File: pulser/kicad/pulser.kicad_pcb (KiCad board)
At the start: 2 copper layers, 90 x 70 mm, 46 parts, among them J1 Screw_Terminal_01x02, J2 Screw_Terminal_01x02, J3 Conn_01x06_Male, J4 Screw_Terminal_01x02, J5 Conn_01x07_Male, Q1 RQ6E080AJTCR, Q2 RQ6E080AJTCR, SW1 SW_Push, SW2 SW_Push, SW3 SW_Push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

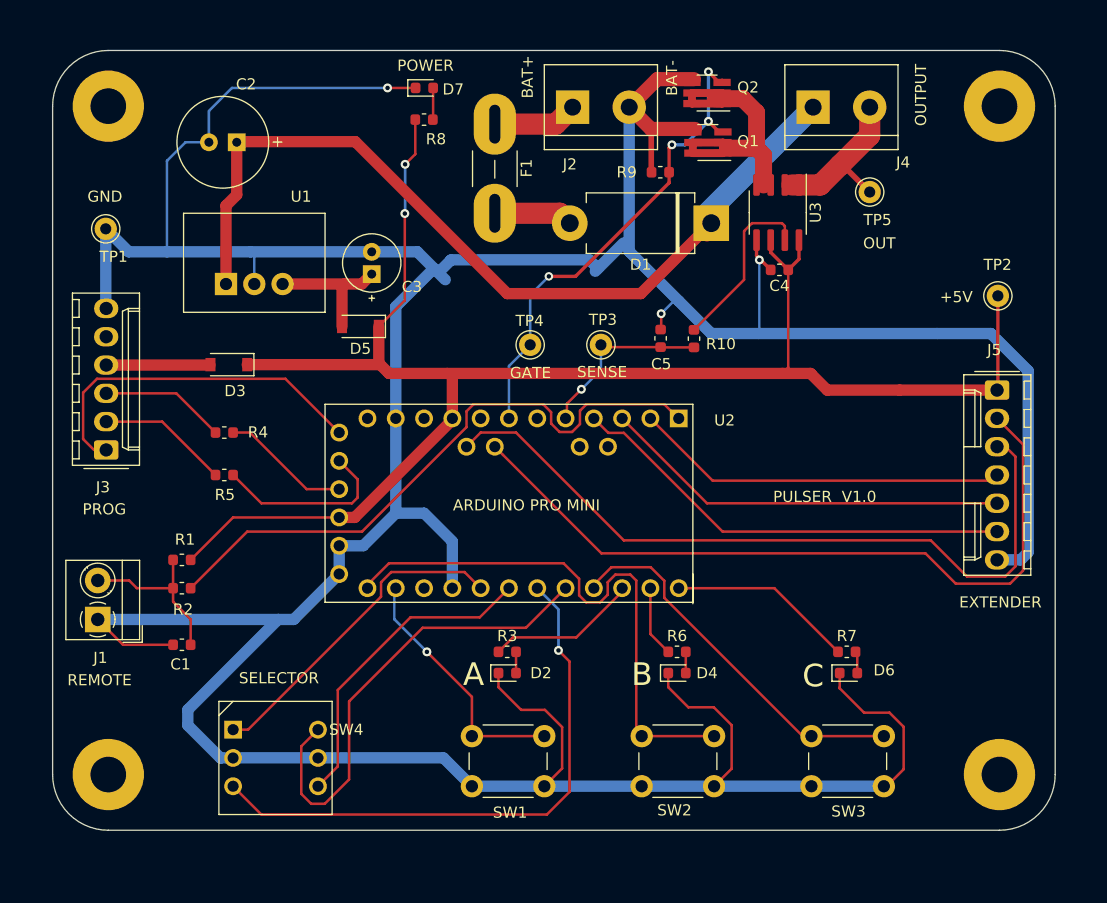
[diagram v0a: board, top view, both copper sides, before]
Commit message: Cleaned up and generted ground plane.
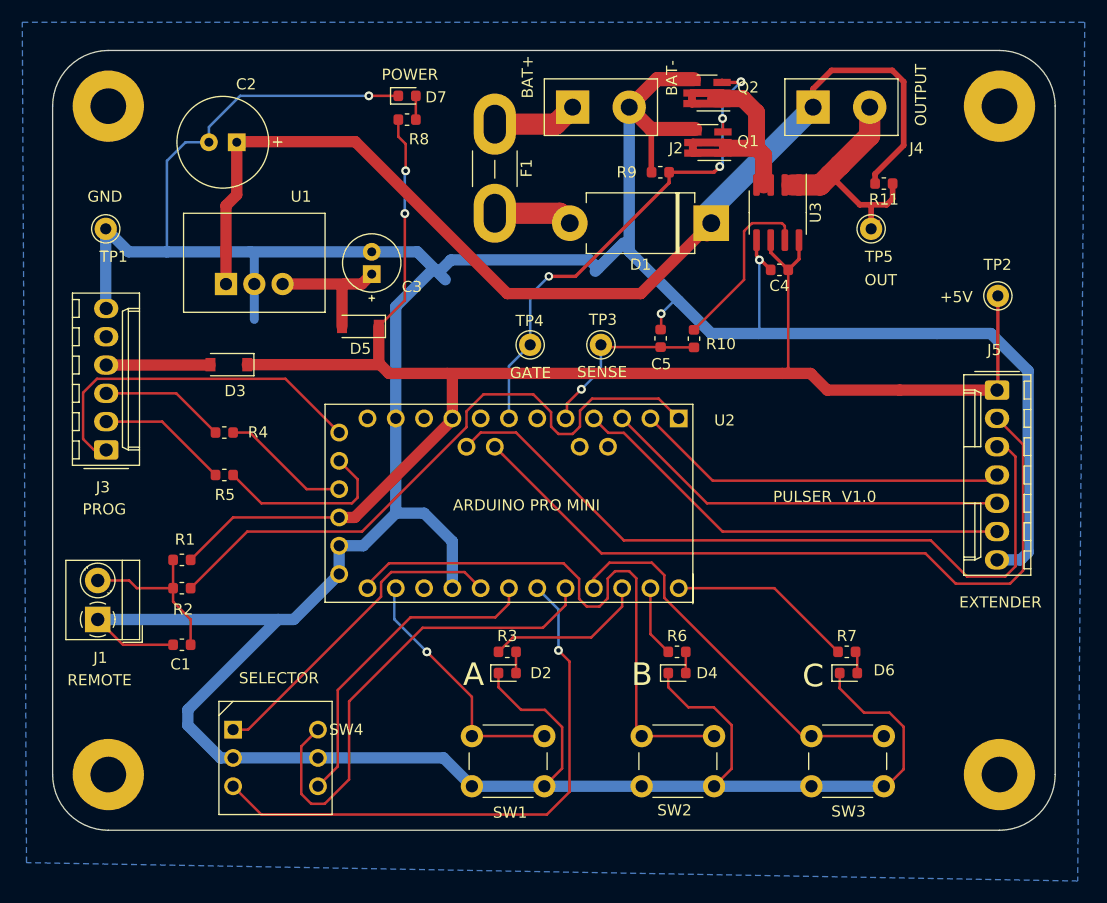
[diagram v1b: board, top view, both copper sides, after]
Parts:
- added R11: 5K, Resistor_SMD:R_0603_1608Metric, F.Cu at (134.6, 91.9)
- F1: footprint pulsar:Fuse_Blade_Mini_directSolder -> Fuse:Fuse_Blade_Mini_directSolder
- J2, J4: footprint TerminalBlock:TerminalBlock_bornier-2_P5.08mm -> pulsar:TerminalBlock_bornier-2_P5.08mm
- Q1, Q2: value RQ6E080AJTCR -> DMN1019UVT-7
- moved TP5 3.30 mm to (133.5, 96.0)
- moved D7 1.70 mm to (91.8, 84.1)
- moved R8 1.52 mm to (91.8, 86.2)
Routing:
- net /+24V: track 77.6 -> 98.7 mm
- net Net-(J4-Pad2): track 15.0 -> 24.0 mm
- net /GATE: track 45.0 -> 47.6 mm
- net /REMOTE: track 55.4 -> 57.0 mm
- net /SW2: track 50.1 -> 51.4 mm
- net /SW3: track 34.2 -> 35.1 mm
- net /ROT8: track 42.6 -> 43.5 mm
- net /ROT2: track 28.5 -> 29.3 mm
- net /LED1: track 13.6 -> 14.4 mm
- net Net-(D7-Pad2): track 2.86 -> 2.17 mm
- added copper zone on B.Cu, net GND
